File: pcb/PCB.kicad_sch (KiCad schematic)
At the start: 4 parts

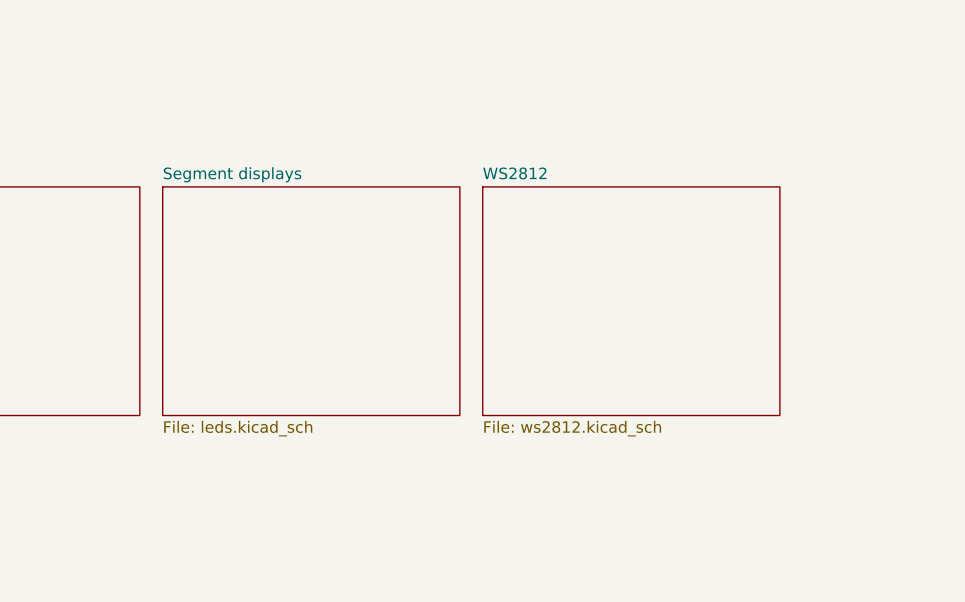
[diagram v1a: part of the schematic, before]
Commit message: Started work on discrete led displays
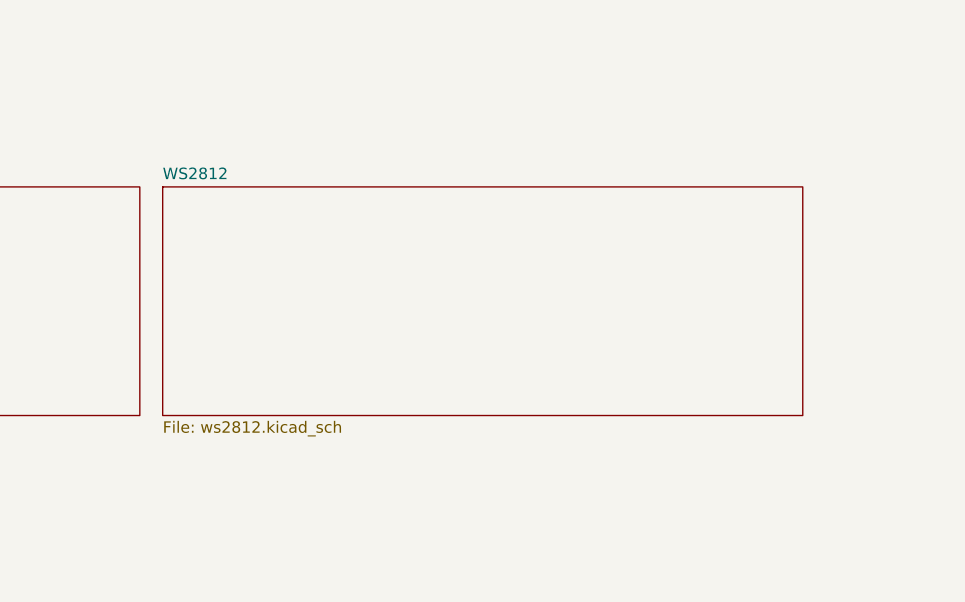
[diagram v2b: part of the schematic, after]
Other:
- removed sheet Segment displays
